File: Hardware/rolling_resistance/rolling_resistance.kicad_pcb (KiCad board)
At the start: 2 copper layers, 14 parts, among them J1 JST-XH-3, J2 JST-XH-3, U1 LM339

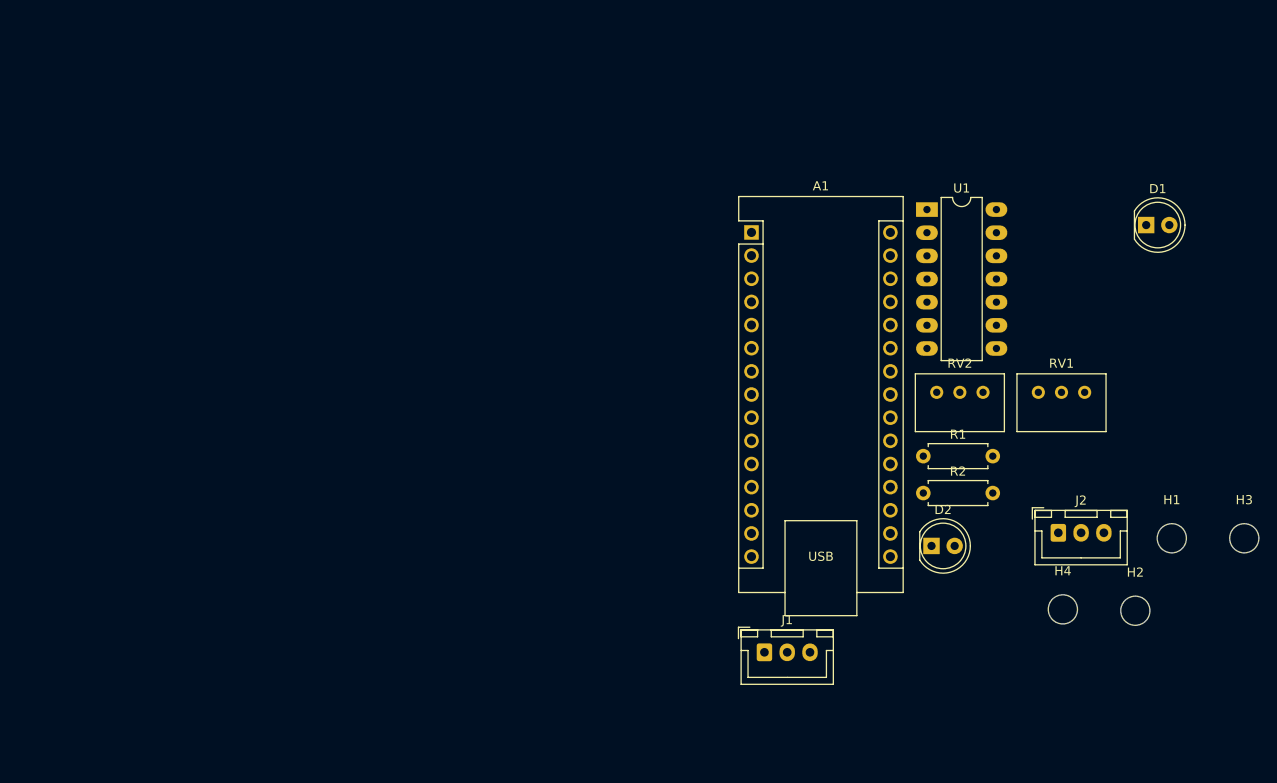
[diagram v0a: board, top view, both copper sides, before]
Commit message: Updated hardware to what was ordered
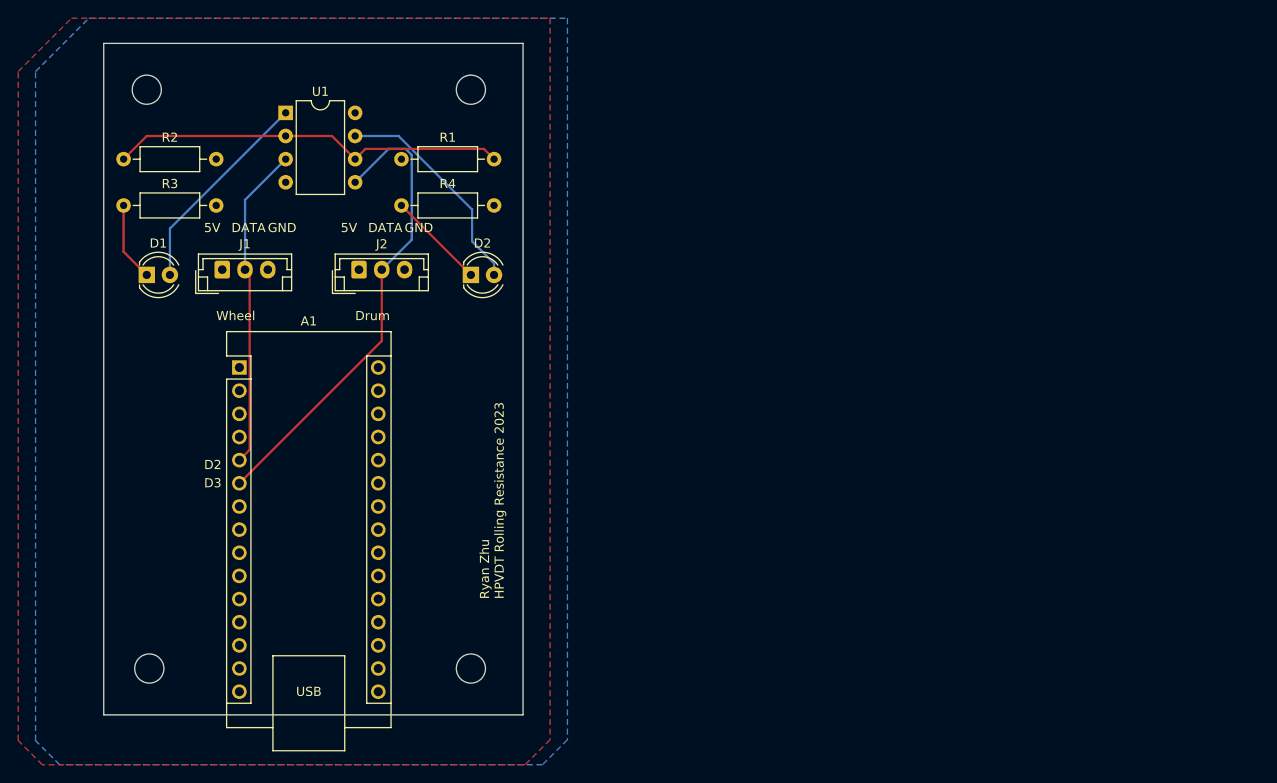
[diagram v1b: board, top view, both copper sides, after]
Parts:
- removed H1, H2, H3, H4: M3, MountingHole:MountingHole_3.2mm_M3
- removed RV1, RV2: 10k, Potentiometer_THT:Potentiometer_Bourns_3299W_Vertical
- added R3: 330, Resistor_THT:R_Axial_DIN0207_L6.3mm_D2.5mm_P10.16mm_Horizontal, F.Cu at (48.3, 78.7)
- added R4: 330, Resistor_THT:R_Axial_DIN0207_L6.3mm_D2.5mm_P10.16mm_Horizontal, F.Cu at (78.7, 78.7)
- added REF**: MountingHole_3.2mm_M3, MountingHole:MountingHole_3.2mm_M3, F.Cu at (86.4, 129.5)
- added REF**: MountingHole_3.2mm_M3, MountingHole:MountingHole_3.2mm_M3, F.Cu at (86.4, 66.0)
- added REF**: MountingHole_3.2mm_M3, MountingHole:MountingHole_3.2mm_M3, F.Cu at (50.8, 66.0)
- added REF**: MountingHole_3.2mm_M3, MountingHole:MountingHole_3.2mm_M3, F.Cu at (51.1, 129.5)
- D1, D2: footprint LED_THT:LED_D5.0mm -> LED_THT:LED_D4.0mm
- J1, J2: value JST-XH-3 -> Conn_01x03; footprint Connector_JST:JST_XH_B3B-XH-A_1x03_P2.50mm_Vertical -> Connector_JST:JST_EH_B3B-EH-A_1x03_P2.50mm_Vertical
- R1, R2: value 330 -> 10K; footprint Resistor_THT:R_Axial_DIN0207_L6.3mm_D2.5mm_P7.62mm_Horizontal -> Resistor_THT:R_Axial_DIN0207_L6.3mm_D2.5mm_P10.16mm_Horizontal
- U1: value LM339 -> LM358; footprint Package_DIP:DIP-14_W7.62mm_LongPads -> Package_DIP:DIP-8_W7.62mm
- moved D1 109.8 mm to (50.8, 86.4)
- moved R2 95.1 mm to (48.3, 73.7)
- moved J2 82.0 mm to (74.1, 85.8)
- moved J1 72.8 mm to (59.1, 85.8)
- moved U1 71.1 mm to (66.0, 68.6)
- moved R1 65.9 mm to (78.7, 73.7)
- moved D2 58.6 mm to (86.4, 86.4)
- moved A1 58.1 mm to (61.0, 96.5)
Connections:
- A1 pad 5: /CMP_{TOP} -> /UPPER
- A1 pad 6: /CMP_{BOT} -> /LOWER
- D1 pad 1: Net-(D1-Pad1) -> Net-(D1-K)
- D1 pad 2: /CMP_{BOT} -> Net-(D1-A)
- D2 pad 1: Net-(D2-Pad1) -> Net-(D2-K)
- D2 pad 2: /CMP_{TOP} -> Net-(D2-A)
- J1 pad 1: GND -> +5V
- J1 pad 2: /IN_{BOT} -> /UPPER
- J1 pad 3: +5V -> GND
- J2 pad 1: GND -> +5V
- J2 pad 2: /IN_{TOP} -> /LOWER
- J2 pad 3: +5V -> GND
- R1 pad 1: Net-(D1-Pad1) -> +5V
- R1 pad 2: GND -> /REF
- R2 pad 1: Net-(D2-Pad1) -> /REF
- U1 pad 1: /CMP_{TOP} -> Net-(D1-A)
- U1 pad 2: /CMP_{BOT} -> /REF
- U1 pad 3: +5V -> /UPPER
- U1 pad 4: /REF_{BOT} -> GND
- U1 pad 5: /IN_{BOT} -> /LOWER
- U1 pad 6: /REF_{TOP} -> /REF
- U1 pad 7: /IN_{TOP} -> Net-(D2-A)
- U1 pad 8: unconnected-(U1-Pad8) -> +5V
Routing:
- net /LOWER: track 0.00 -> 51.9 mm
- net /REF: track 0.00 -> 43.7 mm
- net /UPPER: track 0.00 -> 35.5 mm
- net Net-(D2-A): track 0.00 -> 24.3 mm
- net Net-(D1-A): track 0.00 -> 23.0 mm
- net Net-(D2-K): track 0.00 -> 10.8 mm
- net Net-(D1-K): track 0.00 -> 8.67 mm
- added copper zone on F.Cu, net +5V
- added copper zone on B.Cu, net GND
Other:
- board outline added: 46 x 73.7 mm
- board text added: "5V"
- board text added: "D2"
- board text added: "D3"
- board text added: "DATA"
- board text added: "Drum"
- board text added: "GND"
- board text added: "Ryan Zhu HPVDT Rolling Resistance 2023"
- board text added: "Wheel"
